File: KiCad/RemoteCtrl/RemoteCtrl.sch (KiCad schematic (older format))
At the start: 27 parts, among them J1 UI

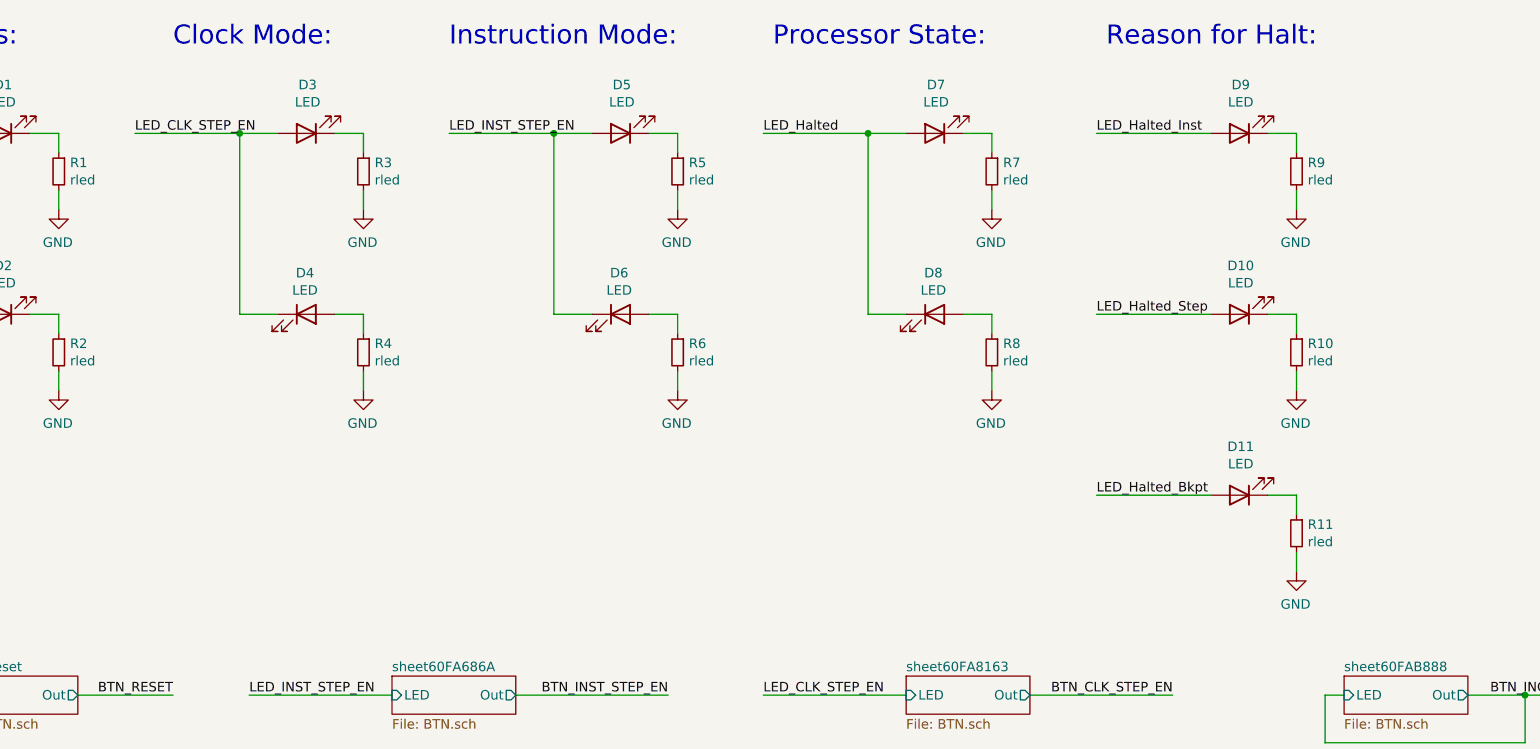
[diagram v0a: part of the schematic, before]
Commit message: Rough layout of Remote finished.
    Did not do connector yet, in case that changes with
    psMCU layout.
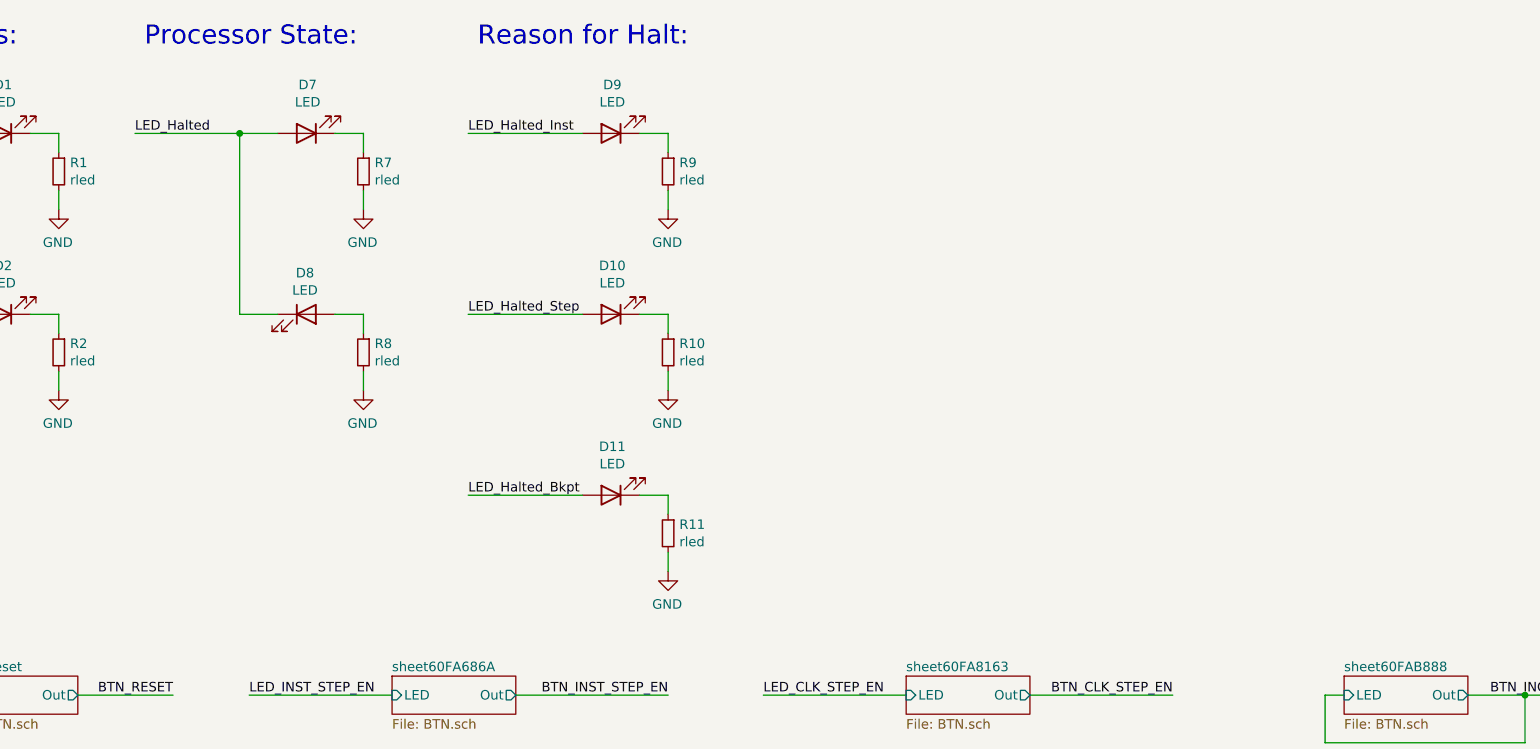
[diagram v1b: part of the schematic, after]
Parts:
- removed D3, D4, D5, D6: LED, LED_THT:LED_D3.0mm, symbol Device:LED
- removed R3, R4, R5, R6: rled, Resistor_SMD:R_0603_1608Metric, symbol Device:R_Small
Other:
- note removed: "Clock Mode:"
- note removed: "Instruction Mode:"
- moved on the sheet: D10, D11, D7, D8, D9, R10, R11, R7, R8, R9
